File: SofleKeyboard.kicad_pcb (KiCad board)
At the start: 2 copper layers, 143.5 x 111.7 mm, 83 parts, among them J3 OLED, SW1 SW_PUSH_LED, SW10 SW_PUSH_LED, SW11 SW_PUSH_LED, SW12 SW_PUSH_LED, SW13 SW_PUSH_LED, SW14 SW_PUSH_LED, SW15 SW_PUSH_LED, SW16 SW_PUSH_LED, SW17 SW_PUSH_LED, SW18 SW_PUSH_LED, SW19 SW_PUSH_LED, SW2 SW_PUSH_LED, SW20 SW_PUSH_LED, SW21 SW_PUSH_LED, SW22 SW_PUSH_LED, SW23 SW_PUSH_LED, SW24 SW_PUSH_LED, SW26 SW_PUSH_LED, SW27 SW_PUSH_LED, SW28 SW_PUSH_LED, SW29 SW_PUSH_LED, SW3 SW_PUSH_LED, SW30 SW_PUSH_LED, SW4 SW_PUSH_LED, SW5 SW_PUSH_LED, SW6 SW_PUSH_LED, SW7 SW_PUSH_LED, SW8 SW_PUSH_LED, SW9 SW_PUSH_LED, U1 ProMicro

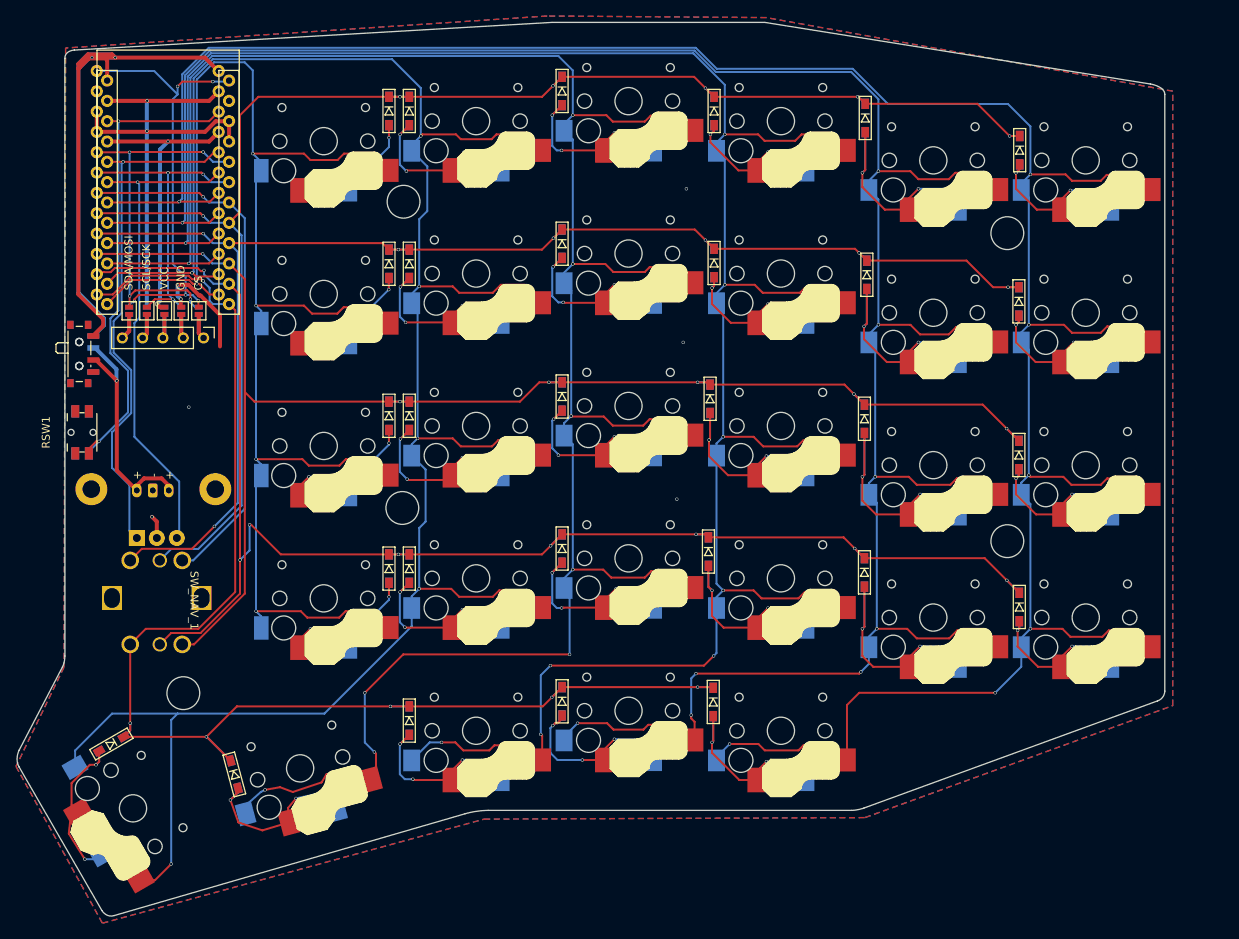
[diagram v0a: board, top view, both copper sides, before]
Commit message: add branding and logo
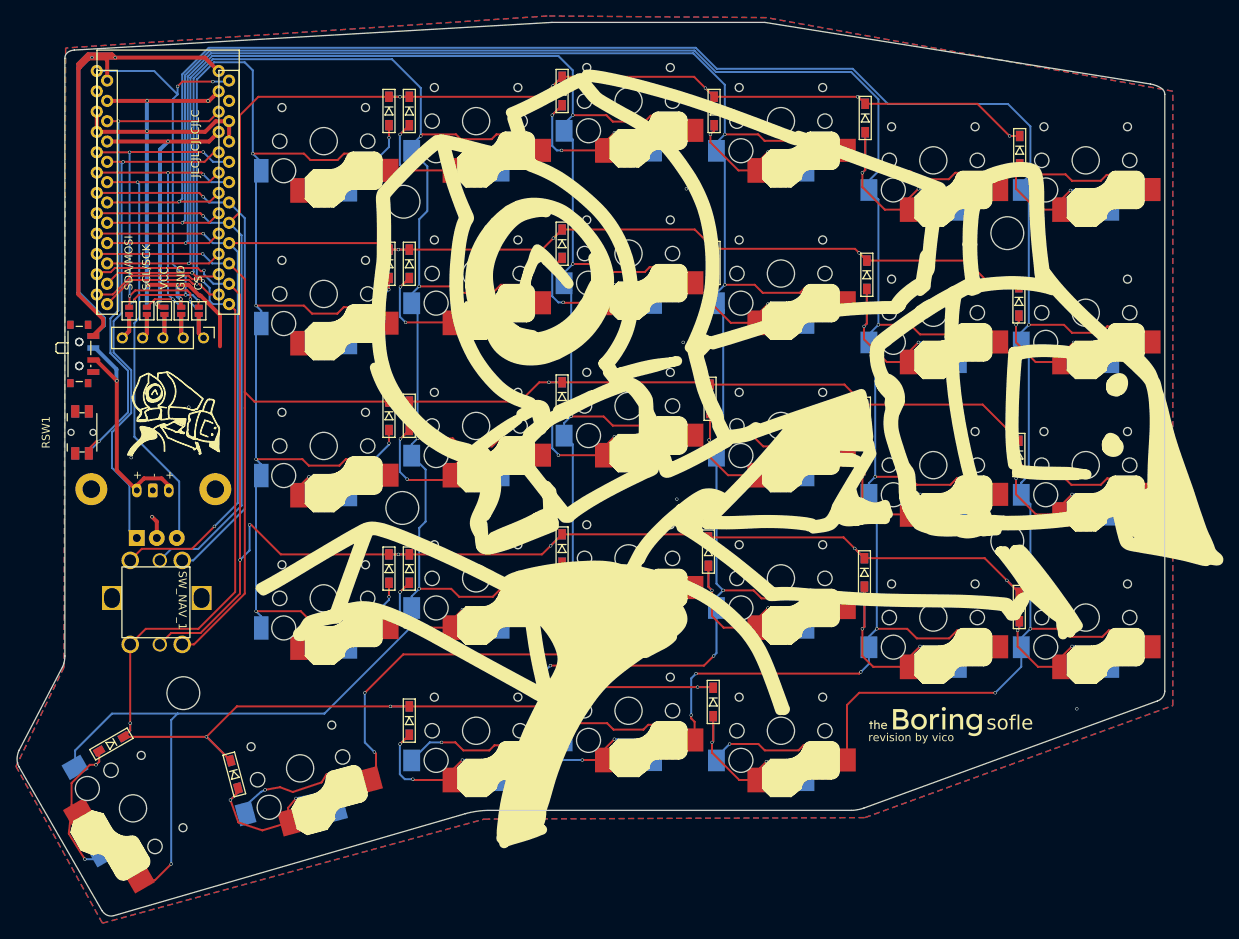
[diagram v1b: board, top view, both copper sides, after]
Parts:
- added REF**: logo_v1_small, VicoKeyboard:logo_v1_small, F.Cu at (166.5, 42.9)
- added REF**: logo_v1_big, VicoKeyboard:logo_v1_big, F.Cu at (235.7, 91.1)
- added REF**: boring_sofle_text, VicoKeyboard:boring_sofle_text, F.Cu at (262.1, 77.5)
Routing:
- net GND: track 79.1 -> 82.9 mm, vias 9 -> 13
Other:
- board text added: "JLCJLCJLCJLC"

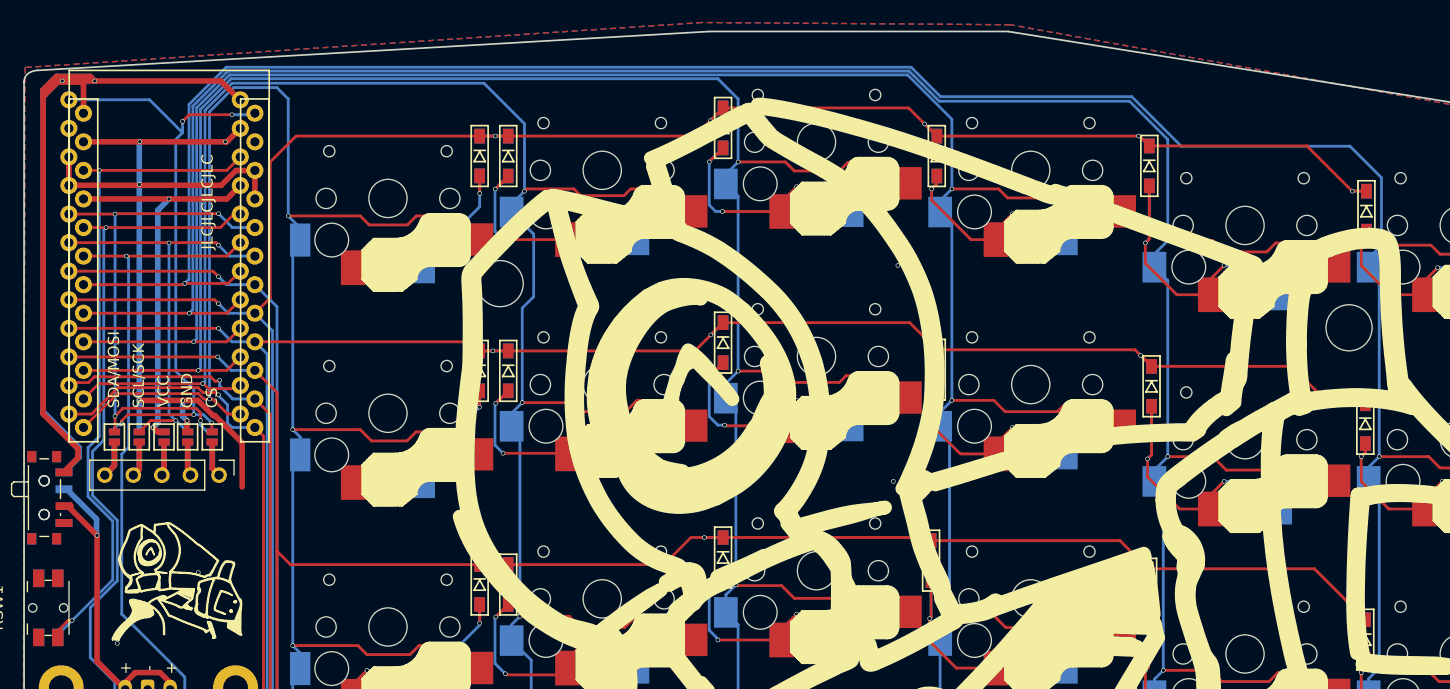
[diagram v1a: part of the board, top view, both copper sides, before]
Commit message: update constraints, switch to 0.127mm track clearance
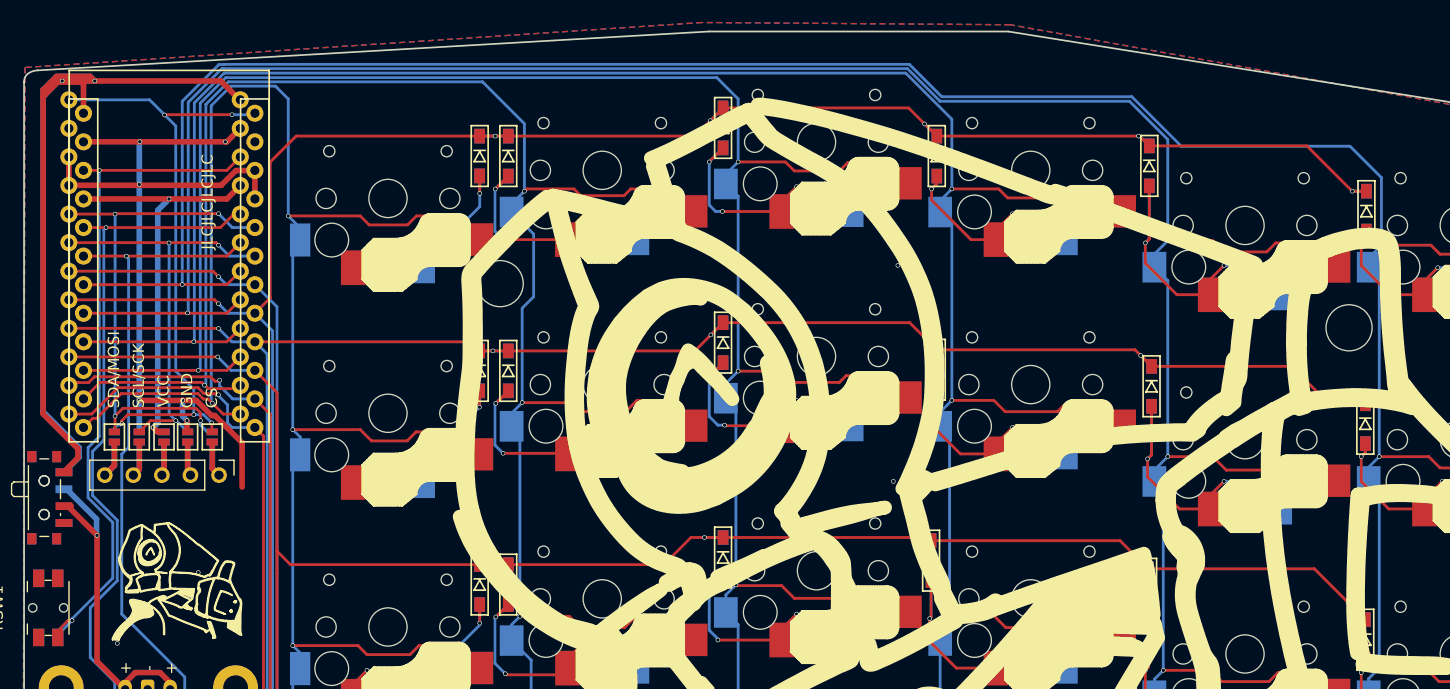
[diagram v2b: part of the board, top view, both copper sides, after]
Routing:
- net col0: track 329.1 -> 330.1 mm
- net col5: track 195.0 -> 195.6 mm
- net col1: track 314.3 -> 315.0 mm
- net col4: track 283.7 -> 284.2 mm
- net col2: track 299.0 -> 299.5 mm
